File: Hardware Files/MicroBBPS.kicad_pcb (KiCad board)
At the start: 2 copper layers, 19.1 x 30.5 mm, 12 parts, among them J1 Conn_02x02_Odd_Even, J2 USB_B_Micro, J3 Conn_02x02_Odd_Even, J4 Conn_01x09, SW1 SW_SPDT, U1 AZ1117-3.3, U2 CP2102N-A01-GQFN24

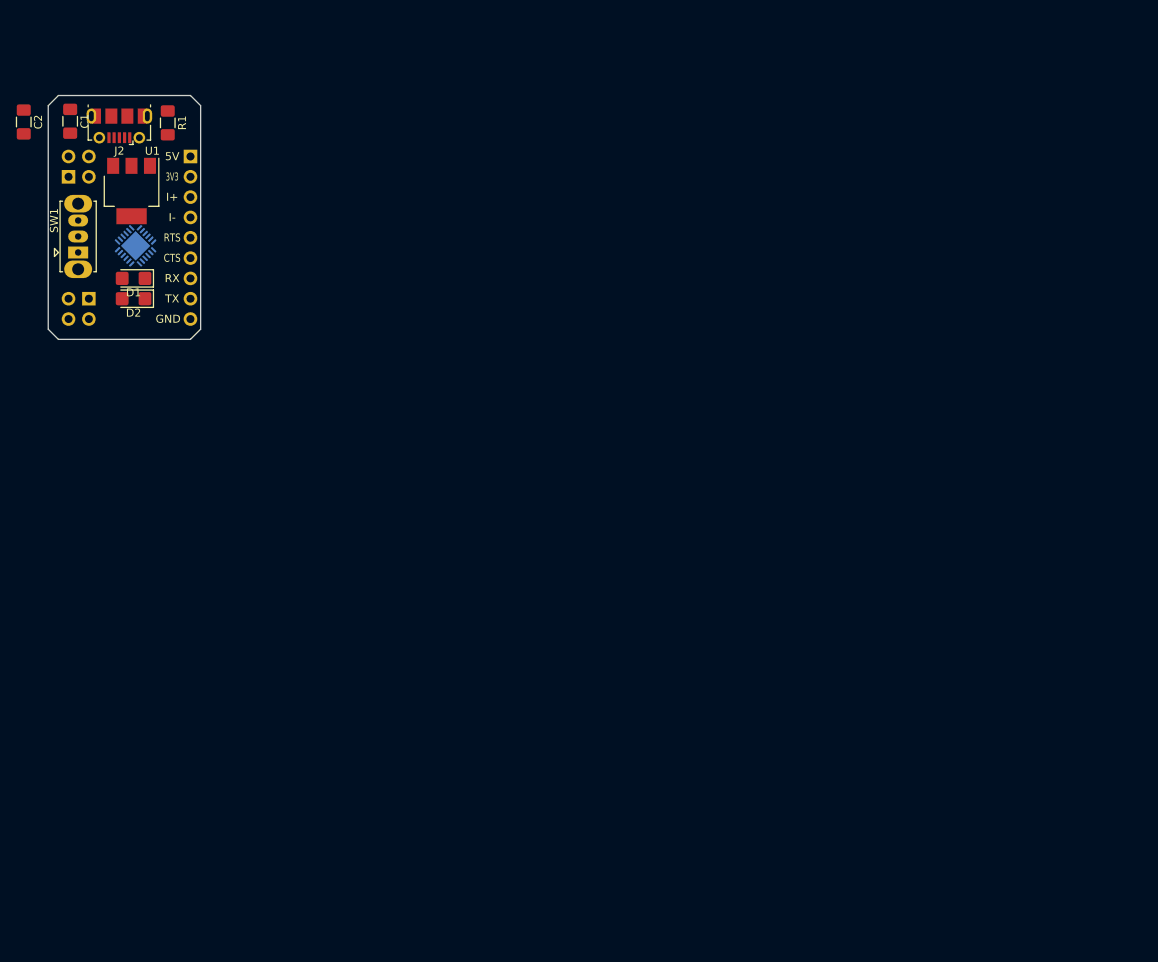
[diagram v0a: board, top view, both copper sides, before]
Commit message: Change board size to full breadboard length Move around components add 5v regulator add input terminal
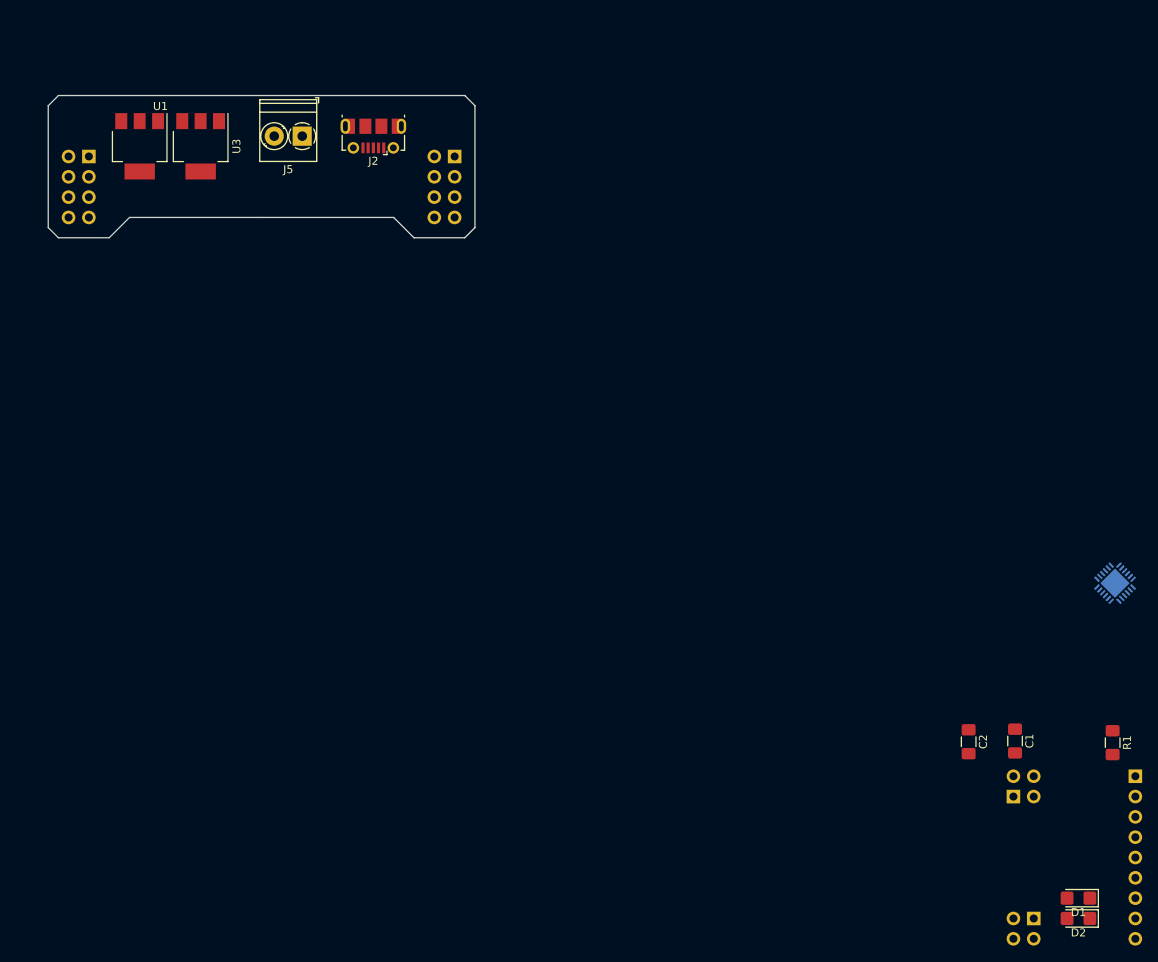
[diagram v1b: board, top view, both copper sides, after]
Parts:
- removed SW1: SW_SPDT, Button_Switch_THT:SW_Slide_1P2T_CK_OS102011MS2Q
- added J5: Conn_01x02, TerminalBlock_Phoenix:TerminalBlock_Phoenix_PT-1,5-2-3.5-H_1x02_P3.50mm_Horizontal, F.Cu at (29.2, -2.54)
- added J6: Conn_02x04_Counter_Clockwise, Connector_PinHeader_2.54mm:PinHeader_2x04_P2.54mm_Vertical, B.Cu at (2.54, 0.00)
- added J7: Conn_02x04_Counter_Clockwise, Connector_PinHeader_2.54mm:PinHeader_2x04_P2.54mm_Vertical, B.Cu at (48.3, 0.00)
- added U3: AZ1117-3.3, Package_TO_SOT_SMD:SOT-223-3_TabPin2, F.Cu at (16.5, -1.27)
- U1: value AZ1117-3.3 -> AZ1117-5.0
- moved C1 141.3 mm to (118.3, 73.1)
- moved C2 141.3 mm to (112.5, 73.2)
- moved D1 141.3 mm to (126.2, 92.7)
- moved D2 141.3 mm to (126.2, 95.2)
- moved J1 141.3 mm to (118.1, 80.0)
- moved J3 141.3 mm to (120.7, 95.2)
- moved J4 141.3 mm to (133.3, 77.5)
- moved R1 141.3 mm to (130.5, 73.3)
- moved U2 129.5 mm to (130.8, 53.3)
- moved J2 31.8 mm to (38.1, -2.54)
- moved U1 5.68 mm to (8.89, -1.27)
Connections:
- net Net-(J2-Pad2) renamed /USB_Conn_D-
- net Net-(J2-Pad3) renamed /USB_Conn_D+
- C1 pad 1: +5V -> VS
- C2 pad 1: +3V3 -> +5V
- J2 pad 1: Net-(J2-Pad1) -> +5V
- U1 pad 2: +3V3 -> Net-(F1-Pad2)
- U1 pad 3: +5V -> VS
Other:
- board size 19.1 x 30.5 mm -> 53.3 x 17.8 mm
- board text removed: "3V3"
- board text removed: "5V"
- board text removed: "CTS"
- board text removed: "GND"
- board text removed: "I+"
- board text removed: "I-"
- board text removed: "RTS"
- board text removed: "RX"
- board text removed: "TX"

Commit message: update layout add artwork update footprints
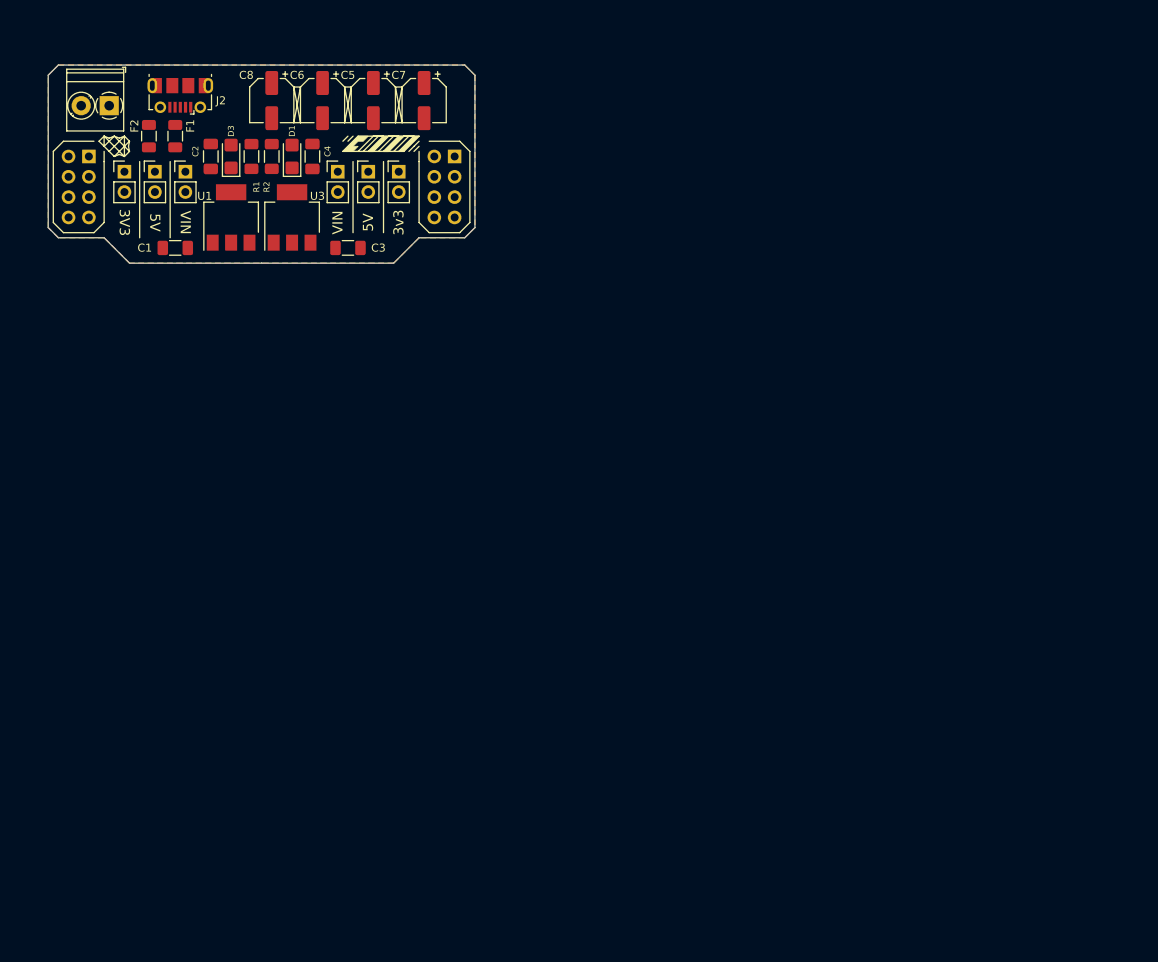
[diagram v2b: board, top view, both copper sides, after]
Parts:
- removed D2: LED, Diode_SMD:D_1206_3216Metric_Castellated
- removed U2: CP2102N-A01-GQFN24, Package_DFN_QFN:QFN-24-1EP_4x4mm_P0.5mm_EP2.6x2.6mm
- added C3: C, Capacitor_SMD:C_1206_3216Metric_Pad1.33x1.80mm_HandSolder, F.Cu at (34.9, 11.4)
- added C4: C, Capacitor_SMD:C_1206_3216Metric_Pad1.33x1.80mm_HandSolder, F.Cu at (30.5, 0.00)
- added C5: CP, Capacitor_SMD:CP_Elec_5x3, F.Cu at (38.1, -6.99)
- added C6: CP, Capacitor_SMD:CP_Elec_5x3, F.Cu at (31.8, -6.99)
- added C7: CP, Capacitor_SMD:CP_Elec_5x3, F.Cu at (44.5, -6.99)
- added C8: CP, Capacitor_SMD:CP_Elec_5x3, F.Cu at (25.4, -6.99)
- added D3: LED, Diode_SMD:D_1206_3216Metric_Castellated, F.Cu at (20.3, 0.00)
- added F1: Polyfuse, Fuse:Fuse_1206_3216Metric, F.Cu at (13.3, -2.54)
- added F2: Polyfuse, Fuse:Fuse_1206_3216Metric, F.Cu at (10.0, -2.54)
- added G***: LOGO, 8Bit_WiFi_Visualizer_Footprints:logo, B.Cu at (41.2, -8.74)
- added J11: Conn_02x01, Connector_PinHeader_2.54mm:PinHeader_1x02_P2.54mm_Vertical, F.Cu at (33.7, 1.91)
- added J12: Conn_02x01, Connector_PinHeader_2.54mm:PinHeader_1x02_P2.54mm_Vertical, F.Cu at (37.5, 1.91)
- added J13: Conn_02x01, Connector_PinHeader_2.54mm:PinHeader_1x02_P2.54mm_Vertical, F.Cu at (41.3, 1.91)
- added R2: R, Resistor_SMD:R_1206_3216Metric_Pad1.30x1.75mm_HandSolder, F.Cu at (25.4, 0.00)
- C1, C2: footprint Capacitor_SMD:C_1206_3216Metric_Pad1.42x1.75mm_HandSolder -> Capacitor_SMD:C_1206_3216Metric_Pad1.33x1.80mm_HandSolder
- J1, J3: value Conn_02x02_Odd_Even -> Conn_02x01; footprint Connector_PinHeader_2.54mm:PinHeader_2x02_P2.54mm_Vertical -> Connector_PinHeader_2.54mm:PinHeader_1x02_P2.54mm_Vertical; moved to F.Cu
- J4: value Conn_01x09 -> Conn_02x01; footprint Connector_PinHeader_2.54mm:PinHeader_1x09_P2.54mm_Vertical -> Connector_PinHeader_2.54mm:PinHeader_1x02_P2.54mm_Vertical; moved to F.Cu
- R1: footprint Resistor_SMD:R_1206_3216Metric_Pad1.42x1.75mm_HandSolder -> Resistor_SMD:R_1206_3216Metric_Pad1.30x1.75mm_HandSolder
- U1: value AZ1117-5.0 -> NCP1117ST50T3G
- U3: value AZ1117-3.3 -> NCP1117ST33T3G
- moved J3 144.2 mm to (10.8, 1.91), turned to 0 degrees
- moved J4 140.7 mm to (14.6, 1.91), turned to 0 degrees
- moved J1 135.8 mm to (6.99, 1.91)
- moved D1 135.1 mm to (27.9, 0.00), turned to 90 degrees
- moved R1 130.2 mm to (22.9, 0.00), turned to 90 degrees
- moved C1 121.7 mm to (13.3, 11.4), turned to 180 degrees
- moved C2 119.7 mm to (17.8, 0.00), turned to 90 degrees
- moved J2 24.7 mm to (14.0, -7.62)
- moved J5 24.4 mm to (5.08, -6.35)
- moved U1 14.5 mm to (20.3, 7.62), turned to 90 degrees
- moved U3 14.5 mm to (27.9, 7.62), turned to 90 degrees
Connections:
- net /+3.3V renamed Net-(J4-Pad2)
- D1 pad 2: Net-(D1-Pad2) -> +3V3
- J4 pad 1: +5V -> Net-(J4-Pad1)
- R1 pad 1: +5V -> Net-(D3-Pad1)
- R1 pad 2: Net-(J2-Pad1) -> GND
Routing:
- added copper zone on F.Cu, net GND
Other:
- board size 53.3 x 17.8 mm -> 53.3 x 24.8 mm
- board text added: "3V3"
- board text added: "3v3"
- board text added: "5V"
- board text added: "VIN"

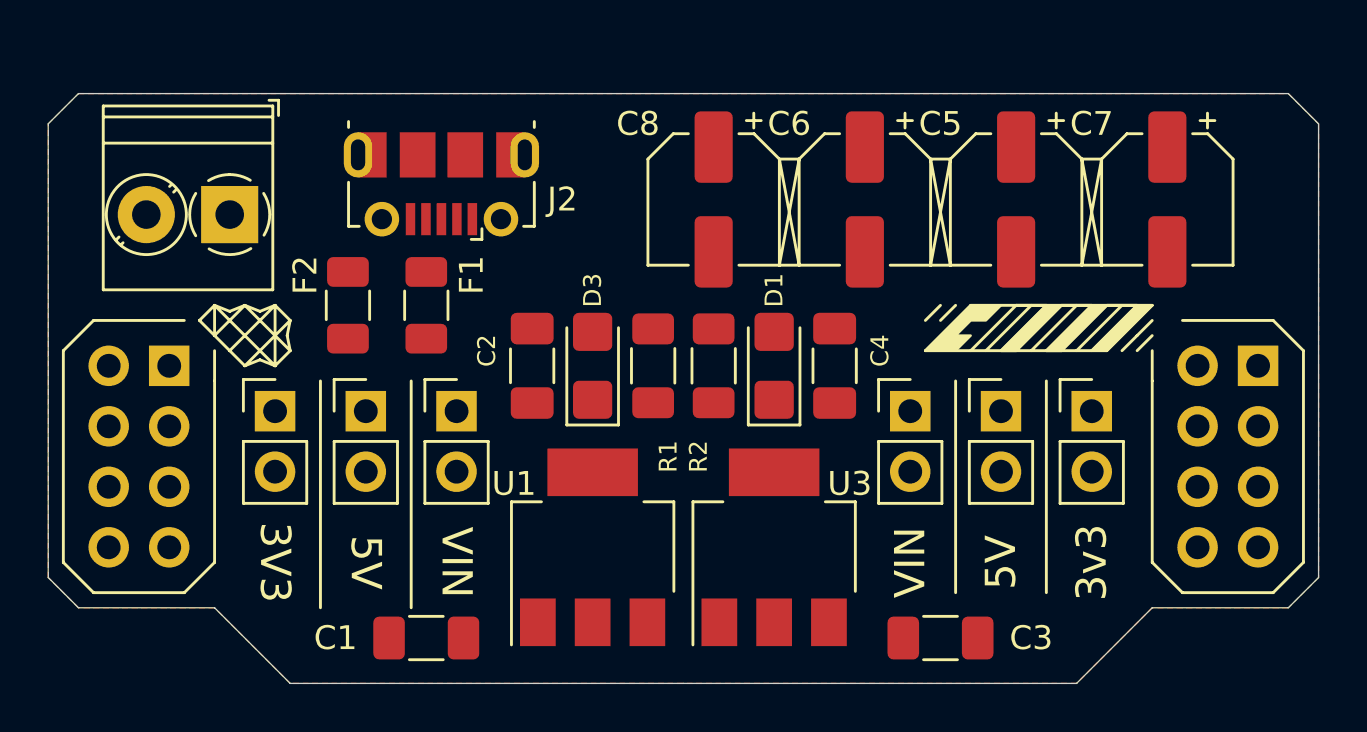
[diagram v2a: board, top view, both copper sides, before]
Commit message: Add footprint library add logos modify board shape add pours route some traces
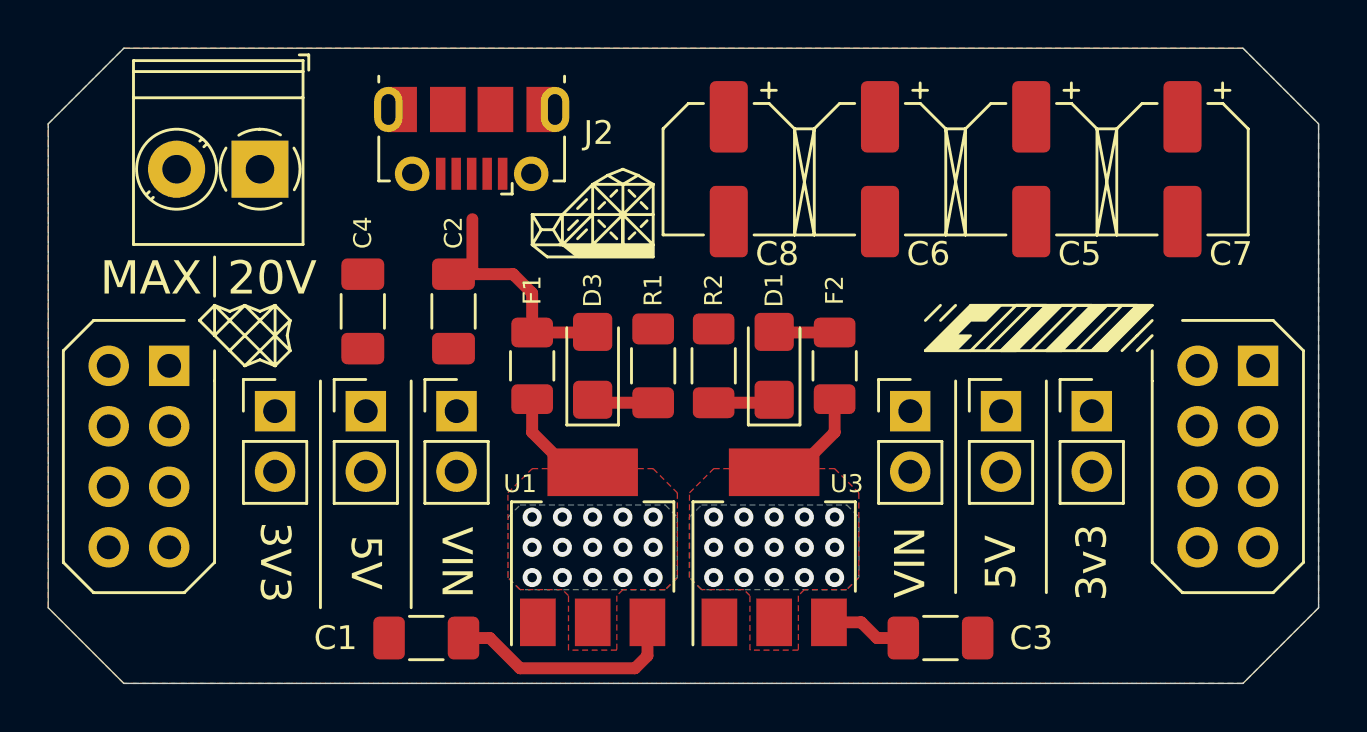
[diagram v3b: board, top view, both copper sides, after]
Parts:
- added G***: LOGO, MicroBBPS:Name Logo, F.Cu at (48.3, -3.17)
- moved G*** 31.4 mm to (10.2, -3.81)
- moved F2 20.6 mm to (30.5, 0.00)
- moved C4 19.9 mm to (10.7, -2.29)
- moved F1 5.12 mm to (17.8, 0.00)
- moved C2 4.02 mm to (14.5, -2.29), turned to 270 degrees
- moved J5 2.29 mm to (6.35, -8.26)
- moved J2 2.29 mm to (15.2, -9.53)
- moved C8 1.42 mm to (26.0, -8.26)
- moved C5 1.42 mm to (38.7, -8.26)
- moved C6 1.42 mm to (32.4, -8.26)
- moved C7 1.42 mm to (45.1, -8.26)
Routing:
- net VS: track 0.00 -> 13.3 mm
- net +5V: track 0.00 -> 10.9 mm
- net Net-(F1-Pad2): track 0.00 -> 4.63 mm, vias 0 -> 15
- net Net-(F2-Pad2): track 0.00 -> 4.63 mm, vias 0 -> 15
- net Net-(D1-Pad1): track 0.00 -> 2.59 mm
- net Net-(D3-Pad1): track 0.00 -> 2.59 mm
- net +3V3: track 0.00 -> 2.55 mm
- added copper zone on B.Cu, net GND
- added copper zone on B.Cu, net Net-(F1-Pad2)
- added copper zone on F.Cu, net Net-(F1-Pad2)
- added copper zone on B.Cu, net Net-(F2-Pad2)
- added copper zone on F.Cu, net Net-(F2-Pad2)
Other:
- board size 53.3 x 24.8 mm -> 53.3 x 26.7 mm
- board text added: "20V"
- board text added: "MAX"

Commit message: add 3D model
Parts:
- removed J1, J11, J12, J13, J3, J4: Conn_02x01, Connector_PinHeader_2.54mm:PinHeader_1x02_P2.54mm_Vertical
- added J8: 3PoleHeaderSwitch, MicroBBPS:3PoleHeaderSwitch, F.Cu at (10.7, 7.62)
- added J9: 3PoleHeaderSwitch, MicroBBPS:3PoleHeaderSwitch, F.Cu at (37.8, 7.62)
- J2: footprint Connector_USB:USB_Micro-B_Molex-105017-0001 -> MicroBBPS:U-F-M5DD-Y-L
- moved J2 1.17 mm to (15.0, -8.38), turned to 0 degrees
- renumbered J6 to Left1, J7 to Right1
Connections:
- Left1 pad 1: Net-(J6-Pad1) -> /VoutLeft
- Left1 pad 3: Net-(J6-Pad3) -> /VoutLeft
- Left1 pad 5: Net-(J6-Pad5) -> /VoutLeft
- Left1 pad 7: Net-(J6-Pad7) -> /VoutLeft
- Right1 pad 1: Net-(J7-Pad1) -> /VoutRight
- Right1 pad 3: Net-(J7-Pad3) -> /VoutRight
- Right1 pad 5: Net-(J7-Pad5) -> /VoutRight
- Right1 pad 7: Net-(J7-Pad7) -> /VoutRight
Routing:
- added copper zone on B.Cu, net /VoutLeft
- added copper zone on B.Cu, net /VoutRight
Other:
- board text removed: "3v3"

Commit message: Change board shape Add more art finalize components finalize placement finalize routing
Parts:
- added D2: D, Diode_SMD:D_SOD-123, F.Cu at (6.99, 3.17)
- added G***: LOGO, MicroBBPS:polarity_rounded_rectangle, F.Cu at (47.0, 11.2)
- added G***: LOGO, MicroBBPS:polarity_rounded_rectangle, F.Cu at (1.27, 11.2)
- added G***: LOGO, MicroBBPS:polarity symbol, F.Cu at (3.05, -14.7)
- added G***: LOGO, MicroBBPS:PCBA Revision, B.Cu at (32.5, 0.00)
- moved G*** 6.71 mm to (15.5, 0.25)
- moved J5 1.52 mm to (4.83, -8.26)
- moved J2 0.76 mm to (15.7, -8.38)
- renumbered C8 to C5, C5 to C7, C7 to C8
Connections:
- C5 pad 1: +3V3 -> +5V
- C7 pad 1: +5V -> +3V3
- J5 pad 1: VS -> Net-(D2-Pad2)
- J9 pad 1: +3V3 -> +5V
- J9 pad 3: +5V -> +3V3
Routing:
- net +3V3: track 2.55 -> 101.8 mm, vias 0 -> 2
- net +5V: track 10.9 -> 80.5 mm
- net VS: track 13.3 -> 63.3 mm, vias 0 -> 1
- net Net-(D2-Pad2): track 0.00 -> 13.2 mm
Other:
- board size 53.3 x 26.7 mm -> 53.3 x 30.1 mm

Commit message: Add part details
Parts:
- C1, C2, C3, C4: value C -> 220nF 50V
- C5, C7: value CP -> 10µF 16V; footprint Capacitor_SMD:CP_Elec_5x3 -> Capacitor_SMD:CP_Elec_4x5.4
- C6, C8: value CP -> 47µF 10V; footprint Capacitor_SMD:CP_Elec_5x3 -> Capacitor_SMD:CP_Elec_4x5.4
- D2: footprint Diode_SMD:D_SOD-123 -> Diode_SMD:D_SMA
- moved C4 22.5 mm to (33.0, 0.00)
- moved D2 7.74 mm to (10.0, -3.94)
- moved G*** 2.43 mm to (13.1, 0.00)
- moved C2 2.41 mm to (15.2, 0.00)
- moved C5 2.01 mm to (27.9, -8.89), turned to 90 degrees
- moved C6 1.42 mm to (33.7, -8.89), turned to 90 degrees
- moved C7 0.90 mm to (39.4, -8.89), turned to 90 degrees
- moved C8 0.63 mm to (45.1, -8.89), turned to 90 degrees
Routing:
- net +3V3: track 101.8 -> 77.4 mm, vias 2 -> 0
- net Net-(D2-Pad2): track 13.2 -> 0.00 mm
- net VS: track 63.3 -> 63.9 mm, vias 1 -> 2
- added copper zone on F.Cu, net Net-(D2-Pad2)
